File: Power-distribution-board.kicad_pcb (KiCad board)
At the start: 4 copper layers, 142.3 x 104.1 mm, 90 parts, among them J1 178.6165.0001 breaker, J10 2606-1104/020-000, J12 2606-1104/020-000, J13 2606-1104/020-000, J15 2606-1104/020-000, J16 2606-1104/020-000, J2 178.6165.0001 breaker, J3 178.6165.0001 breaker, J4 178.6165.0001 breaker, J5 178.6165.0001 breaker, J6 178.6165.0001 breaker, J7 Screw_Terminal_01x03, J9 USB_C_Receptacle_USB2.0_14P, SW1 SW_Nidec_CAS-120A1, U1 ESP32-S3-WROOM-1, U11 TJA1051TK-3, U12 INA220BIDGSR, U13 INA220BIDGSR, U14 INA220BIDGSR, U15 INA220BIDGSR, U16 INA220BIDGSR, U17 INA220BIDGSR, U18 CP2102N-Axx-xQFN24, U2 LM3940IT-3.3, U3 INA220BIDGSR, U4 LM317_SOT-223, U5 TM1637, U6 CC56-12EWA

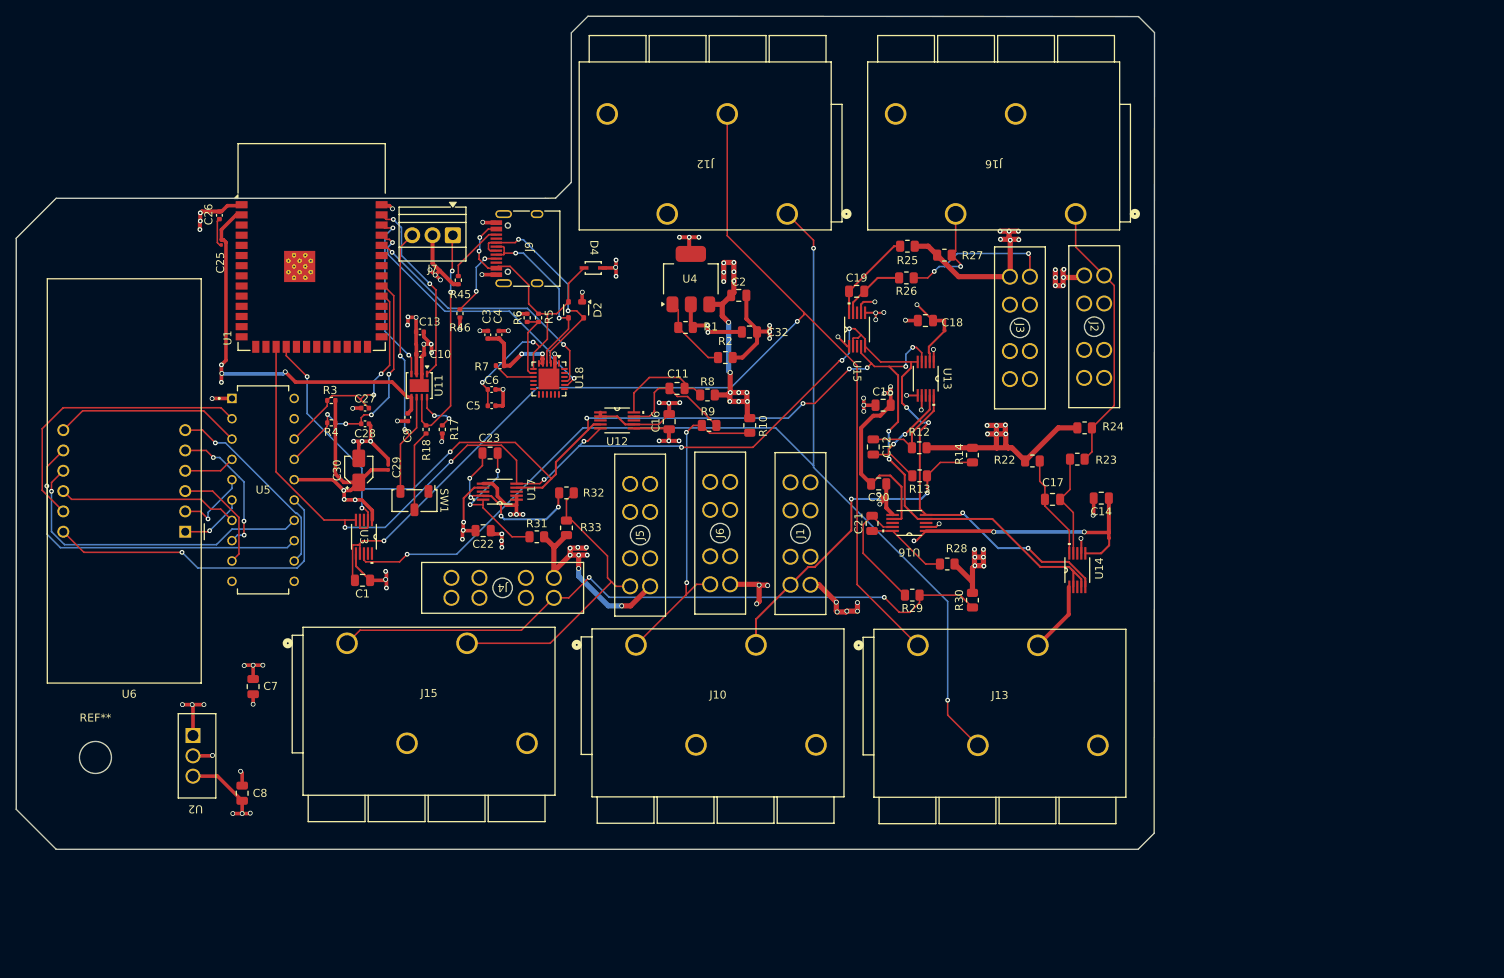
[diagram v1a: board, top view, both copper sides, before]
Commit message: redid layout
implemented some of austens advice. changes:
- correct symbol and footprint used for fuse holders
- correct orientation of usb port
- more compact design?
- placement of current sensors is closer to their respective motor connections
- pwr planes utilize whole board space for heat dissipation

notes -
- need help doing traces. need to figure out how to trace to treat high current optimally
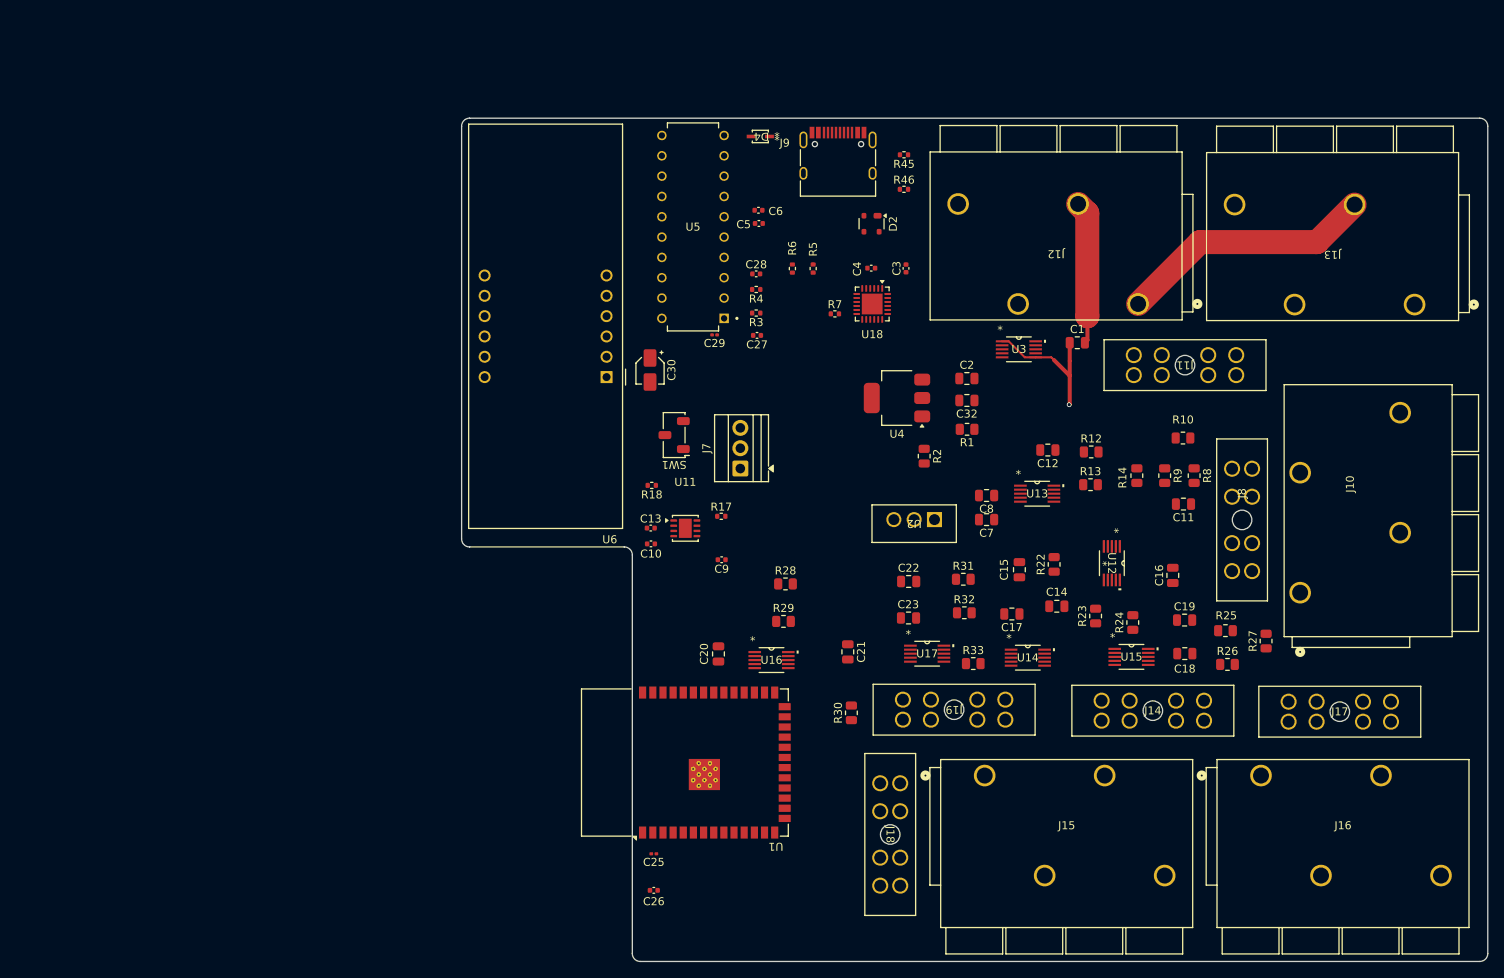
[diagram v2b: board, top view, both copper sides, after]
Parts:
- removed J1, J2, J3, J4, J5, J6: 178.6165.0001 breaker, pdb_footprints:CONN_178.6165.0001_LTF
- removed REF**: MountingHole_4mm, MountingHole:MountingHole_4mm
- added J11: 178.6165.0001, pdb_footprints:CONN_178.6165.0001_LTF, F.Cu at (204.9, 77.9)
- added J14: 178.6165.0001, pdb_footprints:CONN_178.6165.0001_LTF, F.Cu at (213.7, 123.6)
- added J17: 178.6165.0001, pdb_footprints:CONN_178.6165.0001_LTF, F.Cu at (237.1, 123.7)
- added J18: 178.6165.0001, pdb_footprints:CONN_178.6165.0001_LTF, F.Cu at (173.2, 144.2)
- added J19: 178.6165.0001, pdb_footprints:CONN_178.6165.0001_LTF, F.Cu at (176.1, 120.9)
- added J8: 178.6165.0001, pdb_footprints:CONN_178.6165.0001_LTF, F.Cu at (219.7, 92.1)
- moved C26 100.3 mm to (144.9, 144.8), turned to 0 degrees
- moved C8 100.2 mm to (186.5, 95.4), turned to 180 degrees
- moved C1 94.2 mm to (197.9, 76.3), turned to 0 degrees
- moved C7 94.0 mm to (186.5, 98.4), turned to 180 degrees
- moved C25 93.6 mm to (144.9, 140.2), turned to 180 degrees
- moved U2 92.0 mm to (174.9, 99.5), turned to 180 degrees
- moved U3 85.2 mm to (190.6, 77.2), turned to 0 degrees
- moved J10 83.3 mm to (225.7, 107.6), turned to 90 degrees
- moved J15 81.4 mm to (186.3, 130.4)
- moved U1 79.6 mm to (148.8, 128.8), turned to 90 degrees
- moved J13 75.3 mm to (240.0, 71.6), turned to 180 degrees
- moved J16 73.9 mm to (220.8, 130.4), turned to 0 degrees
- moved C16 65.8 mm to (209.8, 105.4)
- moved C11 64.9 mm to (211.1, 96.5)
- moved U12 64.4 mm to (202.2, 103.9), turned to -90 degrees
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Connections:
- R10 pad 1: /MOT1 -> /MOT1_OUT
- R10 pad 2: /BATP -> /MOT1
- R12 pad 2: /BATP -> /MOT2
- R13 pad 1: /MOT2 -> /MOT2_OUT
- R14 pad 1: /MOT2 -> /MOT2_OUT
- R14 pad 2: /BATP -> /MOT2
- R22 pad 2: /BATP -> /MOT3
- R23 pad 1: /MOT3 -> /MOT3_OUT
- R24 pad 1: /MOT3 -> /MOT3_OUT
- R24 pad 2: /BATP -> /MOT3
- R25 pad 2: /BATP -> /MOT4
- R26 pad 1: /MOT4 -> /MOT4_OUT
- R27 pad 1: /MOT4 -> /MOT4_OUT
- R27 pad 2: /BATP -> /MOT4
- R28 pad 2: /BATP -> /MOT5
- R29 pad 1: /MOT5 -> /MOT5_OUT
- R30 pad 1: /MOT5 -> /MOT5_OUT
- R30 pad 2: /BATP -> /MOT5
- R31 pad 2: /BATP -> /MOT6
- R32 pad 1: /MOT6 -> /MOT6_OUT
- R33 pad 1: /MOT6 -> /MOT6_OUT
- R33 pad 2: /BATP -> /MOT6
- R8 pad 2: /BATP -> /MOT1
- R9 pad 1: /MOT1 -> /MOT1_OUT
- U17 pad 1: /5V -> unconnected-(U17-A1-Pad1)
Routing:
- net /SCL: track 173.4 -> 0.00 mm, vias 11 -> 0
- net /SDA: track 172.2 -> 0.00 mm, vias 11 -> 0
- net /BATP: track 156.8 -> 0.00 mm, vias 54 -> 0
- net GND: track 156.7 -> 0.00 mm, vias 49 -> 0
- net /5V: track 159.0 -> 18.0 mm, vias 45 -> 1
- net /AUX-: track 150.7 -> 18.0 mm, vias 2 -> 0
- net /AUX+: track 142.3 -> 32.2 mm, vias 3 -> 0
- net /MOT5: track 85.5 -> 0.00 mm, vias 2 -> 0
- net /3.3V: track 61.6 -> 0.00 mm, vias 7 -> 0
- net Net-(D4-A): track 46.8 -> 0.00 mm, vias 4 -> 0
- net Net-(U5-GRID3): track 43.3 -> 0.00 mm, vias 1 -> 0
- net /MOT2: track 42.0 -> 0.00 mm, vias 2 -> 0
- net /MOT1: track 41.5 -> 0.00 mm, vias 2 -> 0
- net Net-(U5-GRID1): track 40.5 -> 0.00 mm, vias 1 -> 0
- net Net-(U5-GRID2): track 40.5 -> 0.00 mm, vias 1 -> 0
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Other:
- board size 142.3 x 104.1 mm -> 128.3 x 105.4 mm

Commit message: started routing
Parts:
- moved U12 6.14 mm to (208.3, 103.1), turned to 90 degrees
- moved C16 3.05 mm to (212.9, 105.4)
- moved R10 1.90 mm to (212.9, 88.9)
- moved R8 0.38 mm to (212.5, 92.6), turned to 90 degrees
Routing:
- net /MOT2: track 0.00 -> 50.4 mm, vias 0 -> 6
- net /MOT1: track 0.00 -> 50.0 mm, vias 0 -> 5
- net Net-(U12-VIN+): track 0.00 -> 13.4 mm
- net Net-(U12-VIN-): track 0.00 -> 8.75 mm
- net /MOT1_OUT: track 0.00 -> 4.45 mm
- net /BATP: track 0.00 -> 3.31 mm, vias 0 -> 34
- net GND: track 0.00 -> 0.01 mm, vias 0 -> 4
- net /5V: vias 1 -> 4
- added copper zone on F.Cu, net /5V
- added copper zone on F.Cu, net /BATP
- added copper zone on F.Cu, net GND

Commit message: cleaned up repo
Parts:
- removed U4: LM317_SOT-223, Package_TO_SOT_SMD:SOT-223-3_TabPin2
- added REF**: Mounting_Wuerth_WA-SMST-4.5mm_H1mm_9774010982, Mounting_Wuerth:Mounting_Wuerth_WA-SMST-4.5mm_H1mm_9774010982, F.Cu at (243.3, 74.2)
- added REF**: Mounting_Wuerth_WA-SMST-4.5mm_H1mm_9774010982, Mounting_Wuerth:Mounting_Wuerth_WA-SMST-4.5mm_H1mm_9774010982, F.Cu at (246.6, 120.3)
- added REF**: Mounting_Wuerth_WA-SMST-4.5mm_H1mm_9774010982, Mounting_Wuerth:Mounting_Wuerth_WA-SMST-4.5mm_H1mm_9774010982, F.Cu at (149.9, 108.3)
- added REF**: Mounting_Wuerth_WA-SMST-4.5mm_H1mm_9774010982, Mounting_Wuerth:Mounting_Wuerth_WA-SMST-4.5mm_H1mm_9774010982, F.Cu at (174.2, 49.8)
- added U7: LM317_SOT-223, Package_TO_SOT_SMD:SOT-223-3_TabPin2, F.Cu at (179.2, 73.9)
- moved D4 100.9 mm to (169.7, 150.8)
- moved R45 99.5 mm to (149.1, 148.5), turned to 0 degrees
- moved J9 97.0 mm to (158.1, 150.6), turned to 180 degrees
- moved R46 91.2 mm to (149.1, 144.2), turned to 180 degrees
- moved C5 86.6 mm to (167.3, 147.6), turned to 0 degrees
- moved C6 84.4 mm to (167.3, 143.6), turned to 0 degrees
- moved D2 82.0 mm to (153.1, 141.2), turned to 90 degrees
- moved C3 64.1 mm to (166.6, 130.3), turned to -90 degrees
- moved R6 63.6 mm to (169.2, 130.3), turned to -90 degrees
- moved R5 63.3 mm to (164.6, 130.3), turned to -90 degrees
- moved C4 57.4 mm to (165.6, 124.0), turned to 0 degrees
- moved R7 48.0 mm to (170.1, 120.7), turned to 180 degrees
- moved U18 41.9 mm to (159.5, 111.4), turned to 90 degrees
- moved C20 15.7 mm to (167.4, 108.8)
- moved R17 14.6 mm to (167.9, 96.4)
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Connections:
- J10 pad 2: GND -> /BATN
- J10 pad 4: GND -> /BATN
- J13 pad 3: GND -> /BATN
- J15 pad 2: GND -> /BATN
- J15 pad 4: GND -> /BATN
- J16 pad 2: GND -> /BATN
- J16 pad 4: GND -> /BATN
- U17 pad 1: unconnected-(U17-A1-Pad1) -> GND
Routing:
- net GND: track 0.01 -> 176.6 mm, vias 4 -> 24
- net /SDA: track 0.00 -> 148.6 mm, vias 0 -> 8
- net /SCL: track 0.00 -> 140.2 mm, vias 0 -> 11
- net /BATP: track 3.31 -> 135.7 mm, vias 34 -> 23
- net /MOT2: track 50.4 -> 0.00 mm, vias 6 -> 0
- net /MOT1: track 50.0 -> 0.00 mm, vias 5 -> 0
- net /CAN TX: track 0.00 -> 41.8 mm, vias 0 -> 3
- net /CAN RX: track 0.00 -> 33.9 mm, vias 0 -> 2
- net /AUX+: track 32.2 -> 2.02 mm
- net /UART TX: track 0.00 -> 18.5 mm, vias 0 -> 3
- net /UART RX: track 0.00 -> 17.3 mm, vias 0 -> 3
- net /3.3V: track 0.00 -> 15.1 mm, vias 0 -> 5
- net Net-(U12-VIN+): track 13.4 -> 0.00 mm
- net /AUX-: track 18.0 -> 27.8 mm, vias 0 -> 4
- net Net-(U12-VIN-): track 8.75 -> 0.00 mm
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- added copper zone on B.Cu, net /3.3V
- added copper zone on F.Cu, net /AUX+
- added copper zone on In2.Cu, net /AUX-
- added copper zone on In1.Cu, net /BATN
- added copper zone on B.Cu, net /BATP
- added copper zone on In2.Cu, net GND
- removed copper zone on In2.Cu, net /3.3V
- removed copper zone on In2.Cu, net /5V
- removed copper zone on F.Cu, net /BATP
- removed copper zone on In2.Cu, net /BATP
- removed copper zone on F.Cu, net GND
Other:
- board size 128.3 x 105.4 mm -> 123.1 x 118 mm
- board text added: "AUX+"
- board text added: "AUX-"
- board text added: "BAT+"
- board text added: "BAT-"
- board text added: "MOT1"
- board text added: "MOT2"
- board text added: "MOT3"
- board text added: "MOT4"
- board text added: "MOT5"
- board text added: "MOT6"

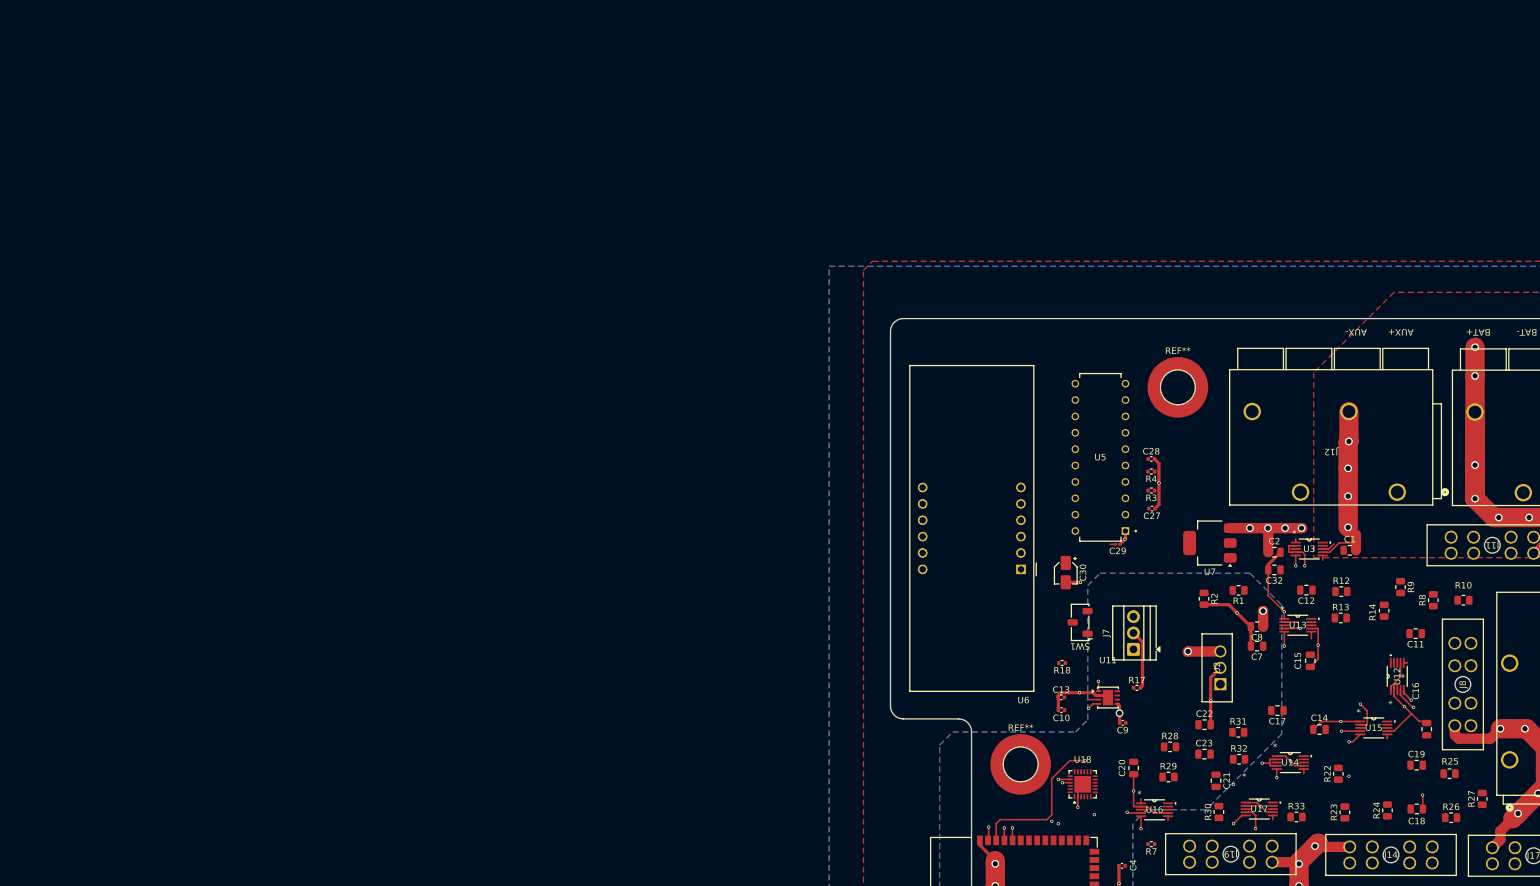
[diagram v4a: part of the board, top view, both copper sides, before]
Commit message: Fixed schematic
-shunt resistor changed to 0.1mO that can handle 8W
-change R10 values to R0 in current sensing circuit
-flip gnd down (convention)
-CAN: get rid of switch; replace with short
-new buck converter for 15v-5v instead of LDO
-updated footprints
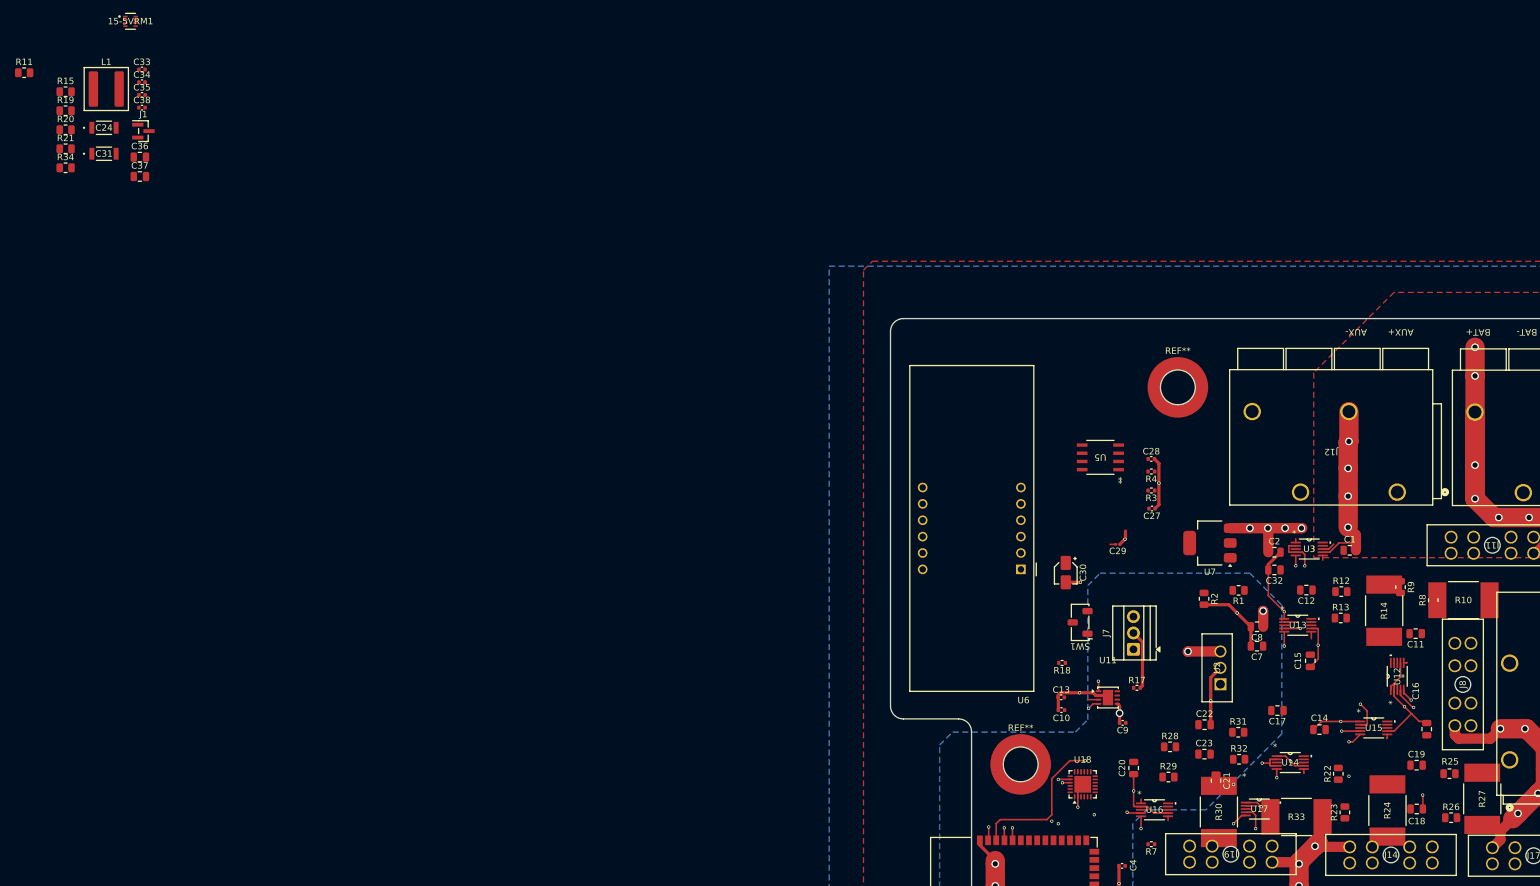
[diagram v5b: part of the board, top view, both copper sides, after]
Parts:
- added 15-5VRM1: TPS62933DRLR, PDB Footprint Library:SOT-5X3-8_DRL_TEX, F.Cu at (11.8, -7.00)
- added C24: 10uF, PDB Footprint Library:CAP_CGA5_TDK-M, F.Cu at (7.66, 9.52)
- added C31: 10uF, PDB Footprint Library:CAP_CGA5_TDK-M, F.Cu at (7.66, 13.5)
- added C33: 100nF, Capacitor_SMD:C_0402_1005Metric, F.Cu at (13.6, 0.48)
- added C34: 33nF, Capacitor_SMD:C_0402_1005Metric, F.Cu at (13.6, 2.46)
- added C35: 100nF, Capacitor_SMD:C_0402_1005Metric, F.Cu at (13.6, 4.42)
- added C36: 22uF, Capacitor_SMD:C_0805_2012Metric, F.Cu at (13.2, 14.1)
- added C37: 22uF, Capacitor_SMD:C_0805_2012Metric, F.Cu at (13.2, 17.1)
- added C38: 100nF, Capacitor_SMD:C_0402_1005Metric, F.Cu at (13.6, 6.39)
- added J1: Conn_01x03_Pin, Connector_PinHeader_1.00mm:PinHeader_1x03_P1.00mm_Vertical_SMD_Pin1Left, F.Cu at (13.8, 10.0)
- added L1: 6.8uH, Inductor_SMD:L_Wuerth_XHMI-6060, F.Cu at (8.02, 3.50)
- added R11: 511k, Resistor_SMD:R_0805_2012Metric, F.Cu at (-4.72, 0.97)
- added R15: 88.7k, Resistor_SMD:R_0805_2012Metric, F.Cu at (1.71, 3.92)
- added R19: 10.2k, Resistor_SMD:R_0805_2012Metric, F.Cu at (1.71, 6.88)
- added R20: 0, Resistor_SMD:R_0805_2012Metric, F.Cu at (1.71, 9.82)
- added R21: 53.55k, Resistor_SMD:R_0805_2012Metric, F.Cu at (1.71, 12.8)
- added R34: 49.9, Resistor_SMD:R_0805_2012Metric, F.Cu at (1.71, 15.7)
- J11, J14, J17, J18, J19, J8: footprint pdb_footprints:CONN_178.6165.0001_LTF -> PDB Footprint Library:CONN_178.6165.0001_LTF
- R10, R14, R24, R27, R30, R33: value 0.01 -> 1m; footprint Resistor_SMD:R_0805_2012Metric -> PDB Footprint Library:RES_3920R_1L00x_BRN-M
- R12, R13, R22, R23, R25, R26, R28, R29, R31, R32, R8, R9: value 10 -> 0
- U2: footprint pdb_footprints:T03B -> PDB Footprint Library:T03B
- U5: footprint pdb_footprints:LED_driver_TM1637 -> PDB Footprint Library:SO8_SOT96-1_NXP-M
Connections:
- C13 pad 1: GND -> /5V
- C13 pad 2: /5V -> GND
- C25 pad 1: Net-(C25-Pad1) -> GND
- C26 pad 2: Net-(C25-Pad1) -> /3.3V
- R18 pad 2: Net-(SW1-B) -> Net-(J7-Pin_3)
- U17 pad 1: GND -> /5V
